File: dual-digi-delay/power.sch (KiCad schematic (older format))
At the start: 8 parts, among them U7 LM7805_TO220

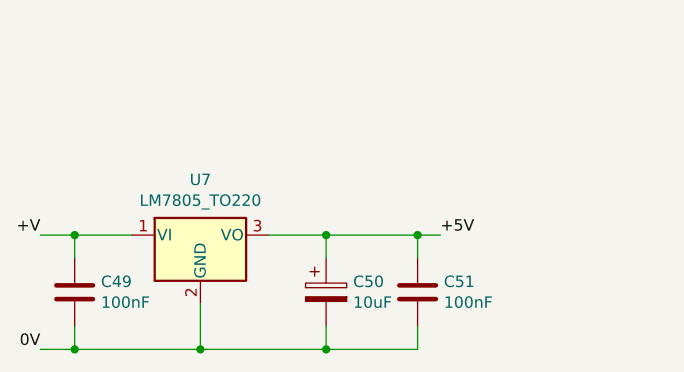
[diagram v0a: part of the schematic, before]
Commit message: Updating digi delay to rev 2
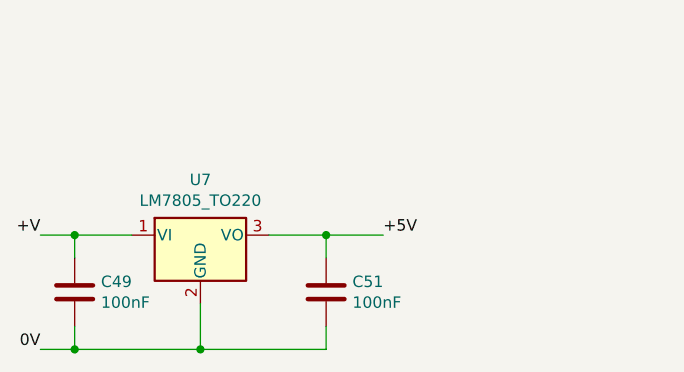
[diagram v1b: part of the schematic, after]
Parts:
- removed C50: 10uF, rumblesan-footprints:CP_Radial_D6.3mm_P2.50mm, symbol Device:CP
- U7: footprint Package_TO_SOT_THT:TO-220-3_Vertical -> Package_TO_SOT_THT:TO-220-3_Horizontal_TabDown
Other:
- moved on the sheet: C51
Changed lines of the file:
@@
 $Descr A4 11693 8268
 encoding utf-8
-Sheet 4 10
+Sheet 4 11
 Title ""
 Date ""
@@
 F 0 "U7" H 4050 3292 50  0000 C CNN
 F 1 "LM7805_TO220" H 4050 3201 50  0000 C CNN
-F 2 "Package_TO_SOT_THT:TO-220-3_Vertical" H 4050 3275 50  0001 C CIN
+F 2 "Package_TO_SOT_THT:TO-220-3_Horizontal_TabDown" H 4050 3275 50  0001 C CIN
 F 3 "https://www.onsemi.cn/PowerSolutions/document/MC7800-D.PDF" H 4050 3000 50  0001 C CNN
 	1    4050 3050
@@
 $EndComp
 $Comp
-L Device:CP C?
-U 1 1 618D0CB8
+L Device:C C?
+U 1 1 618D0CBE
 P 4600 3300
-AR Path="/618D0CB8" Ref="C?"  Part="1"
-AR Path="/618C5F1E/618D0CB8" Ref="C50"  Part="1"
-F 0 "C50" H 4718 3346 50  0000 L CNN
-F 1 "10uF" H 4718 3255 50  0000 L CNN
-F 2 "rumblesan-footprints:CP_Radial_D6.3mm_P2.50mm" H 4638 3150 50  0001 C CNN
+AR Path="/618D0CBE" Ref="C?"  Part="1"
+AR Path="/618C5F1E/618D0CBE" Ref="C51"  Part="1"
+F 0 "C51" H 4485 3254 50  0000 R CNN
+F 1 "100nF" H 4485 3345 50  0000 R CNN
+F 2 "rumblesan-footprints:C_Rect_L7.0mm_W3.5mm_P5.00mm" H 4638 3150 50  0001 C CNN
 F 3 "~" H 4600 3300 50  0001 C CNN
 	1    4600 3300
-	1    0    0    -1
-$EndComp
-$Comp
-L Device:C C?
-U 1 1 618D0CBE
-P 5000 3300
-AR Path="/618D0CBE" Ref="C?"  Part="1"
-AR Path="/618C5F1E/618D0CBE" Ref="C51"  Part="1"
-F 0 "C51" H 4885 3254 50  0000 R CNN
-F 1 "100nF" H 4885 3345 50  0000 R CNN
-F 2 "rumblesan-footprints:C_Rect_L7.0mm_W3.5mm_P5.00mm" H 5038 3150 50  0001 C CNN
-F 3 "~" H 5000 3300 50  0001 C CNN
-	1    5000 3300
 	-1   0    0    1
 $EndComp
@@
 	4350 3050 4600 3050
 Wire Wire Line
-	5000 3050 5000 3150
-Wire Wire Line
 	4600 3150 4600 3050
-Connection ~ 4600 3050
-Wire Wire Line
-	4600 3050 5000 3050
-Wire Wire Line
-	5000 3550 5000 3450
 Wire Wire Line
 	4600 3450 4600 3550
-Connection ~ 4600 3550
-Wire Wire Line
-	4600 3550 5000 3550
 Wire Wire Line
 	4050 3350 4050 3550
@@
 Wire Wire Line
 	4050 3550 4600 3550
-Wire Wire Line
-	5000 3050 5100 3050
-Connection ~ 5000 3050
 Connection ~ 3500 3050
 Wire Wire Line
@@
 Text Label 4000 2000 2    50   ~ 0
 -V
-Text Label 5100 3050 0    50   ~ 0
+Text Label 4850 3050 0    50   ~ 0
 +5V
 Text Label 3350 3050 2    50   ~ 0
@@
 Wire Wire Line
 	4250 1500 4250 1600
+Wire Wire Line
+	4600 3050 4850 3050
+Connection ~ 4600 3050
 $EndSCHEMATC
